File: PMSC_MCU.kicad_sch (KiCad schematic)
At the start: 31 parts, among them J8 ICD, SW4 Push_Button, U8 TM4C123GH6PMTR, Y1 16 MHz, 8 pF GND24

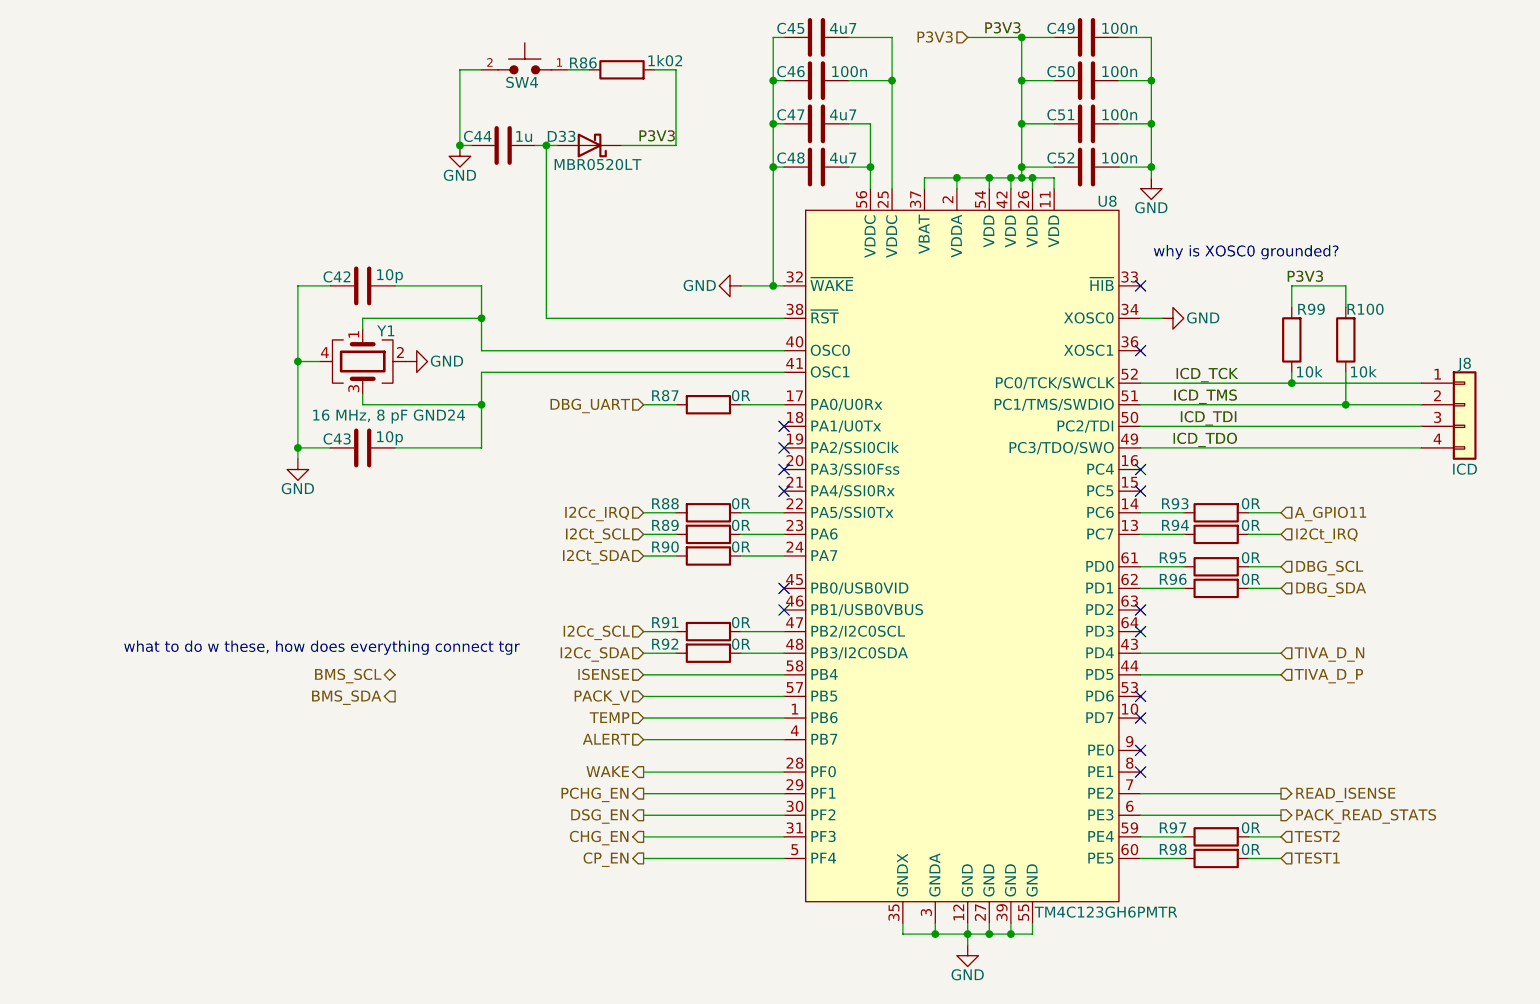
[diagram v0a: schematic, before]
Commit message: commit before simplifying and removing features
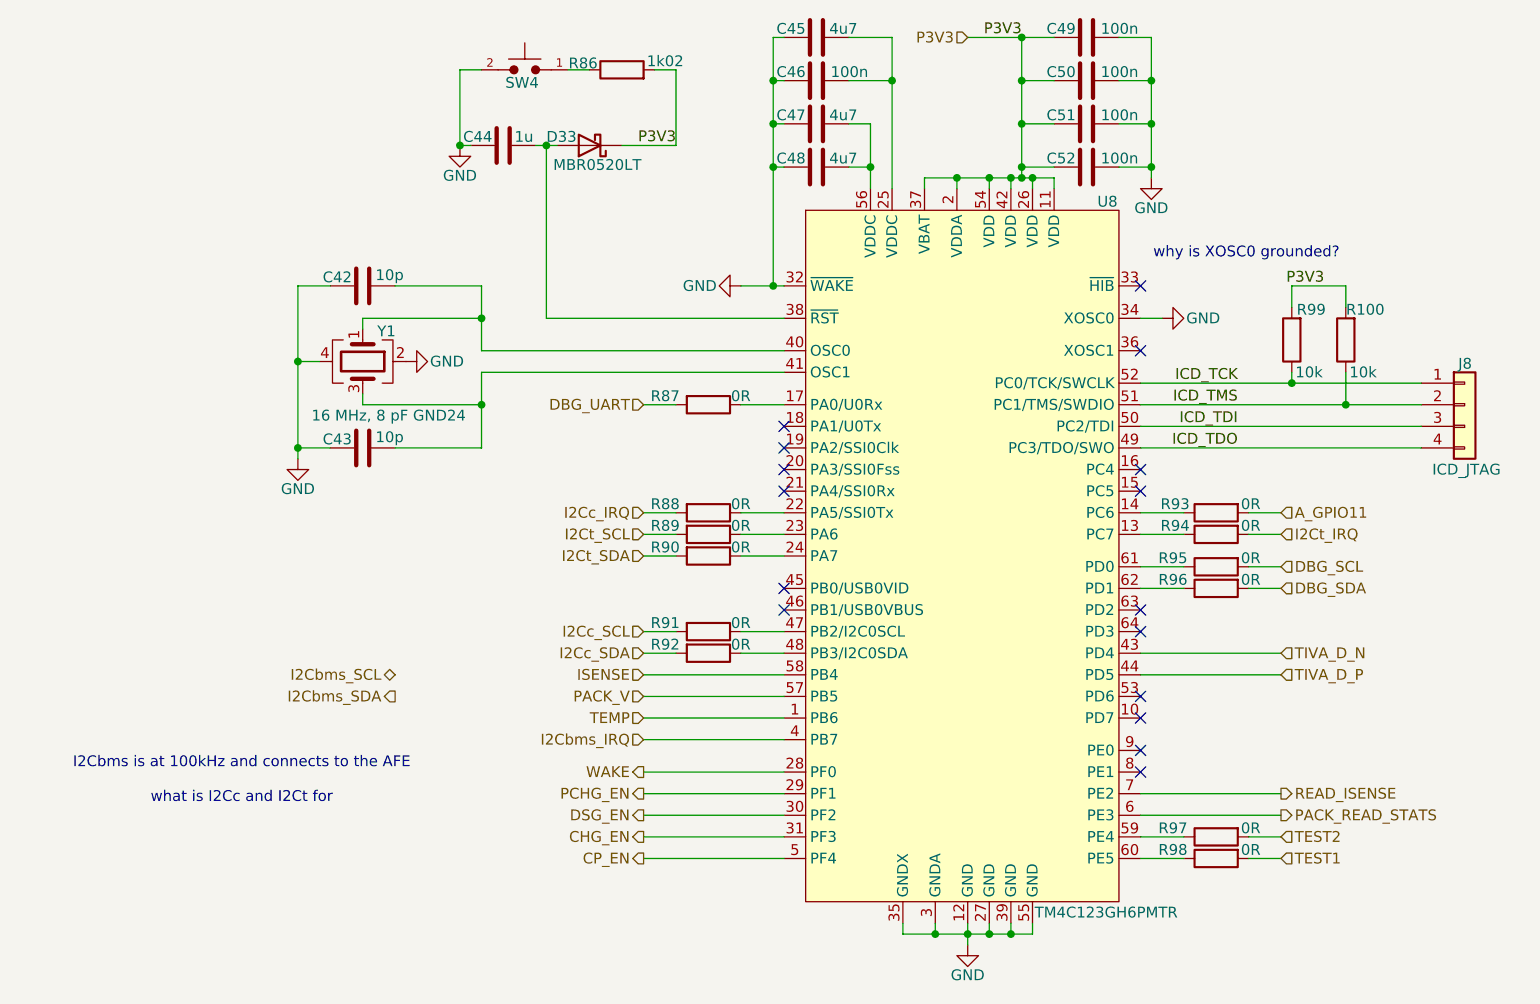
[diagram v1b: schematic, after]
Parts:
- J8: value ICD -> ICD_JTAG
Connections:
- net ALERT renamed I2Cbms_IRQ
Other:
- note added: "I2Cbms is at 100kHz and connects to the AFE what is I2Cc and I2Ct for"
- note removed: "what to do w these, how does everything connect tgr"
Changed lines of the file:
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@@
 	(generator_version "9.0")
 	(paper "A4")
-	(text "what to do w these, how does everything connect tgr"
-		(exclude_from_sim no)
-		(at 67.564 103.632 0)
-		(effects
-			(font
-				(size 1.27 1.27)
-			)
-		)
-	)
 	(text "why is XOSC0 grounded?"
 		(exclude_from_sim no)
@@
 		)
 	)
+	(text "I2Cbms is at 100kHz and connects to the AFE\n\nwhat is I2Cc and I2Ct for"
+		(exclude_from_sim no)
+		(at 58.166 119.126 0)
+		(effects
+			(font
+				(size 1.27 1.27)
+			)
+		)
+	)
 	(junction
 		(at 165.1 46.99)
@@
 		)
 	)
-	(hierarchical_label "BMS_SCL"
+	(hierarchical_label "I2Cbms_SCL"
 		(shape bidirectional)
 		(at 76.2 106.68 180)
@@
 		)
 	)
-	(hierarchical_label "ALERT"
+	(hierarchical_label "I2Cbms_IRQ"
 		(shape input)
 		(at 105.41 114.3 180)
@@
 		)
 	)
-	(hierarchical_label "BMS_SDA"
+	(hierarchical_label "I2Cbms_SDA"
 		(shape output)
 		(at 76.2 109.22 180)
@@
 			)
 		)
-		(property "Value" "ICD"
-			(at 200.406 82.55 0)
-			(effects
-				(font
+		(property "Value" "ICD_JTAG"
+			(at 198.12 82.55 0)
+			(effects
+				(font
